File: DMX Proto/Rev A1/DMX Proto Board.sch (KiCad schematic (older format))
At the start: 20 parts, among them J1 XLR5, J2 XLR5, J3 CONN_01X02_MALE, J4 CONN_01X02_MALE, J5 CONN_01X02_MALE, J6 CONN_01X02_MALE, U1 MAX481, U2 MAX481, U3 TCMT1600, U4 TCMT1600

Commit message: change dmx buffer
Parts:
- removed J3: CONN_01X02_MALE, conn_Molex:7395-02, symbol CONN_01X02_MALE
- removed R3, R4, R6, R8: 1K, Resistors_SMD:R_0603_HandSoldering, symbol R
- removed R5, R7: 4K7, Resistors_SMD:R_0603_HandSoldering, symbol R
- removed U1, U2: MAX481, Housings_SOIC:SOIC-8_3.9x4.9mm_Pitch1.27mm, symbol MAX481
- removed U3, U4: TCMT1600, Housings_SSOP:SOP-4_4.4x2.8mm_Pitch1.27mm, symbol TCMT1600
- added U1, U2: ISO35T, Housings_SOIC:SOIC-16_7.5x10.5mm_Pitch1.27mm, symbol ISO35T
- added U?: TPS76333, TO_SOT_Packages_SMD:SOT-23-5, symbol TPS76333
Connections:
- net labels added: +3.3V, +3.3VA, DMX+, DMX-, GNDA, RDM+, RDM-
- net labels removed: +5V, DMX_IN_A, DMX_IN_B, DMX_OUT_A, DMX_OUT_B, DMX_RX, DMX_TX
- wire segments 87 -> 79
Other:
- moved on the sheet: D1, J1, J2, J4, J6, R1, R2, R9

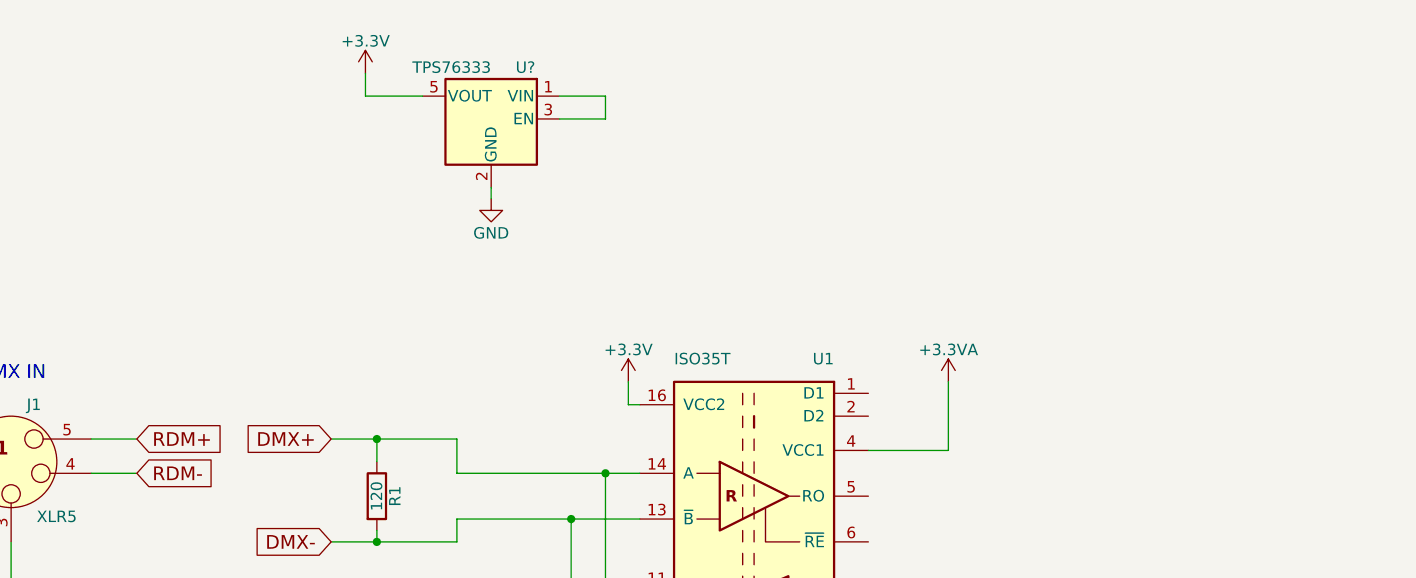
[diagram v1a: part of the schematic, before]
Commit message: Add power isolation to the schematic
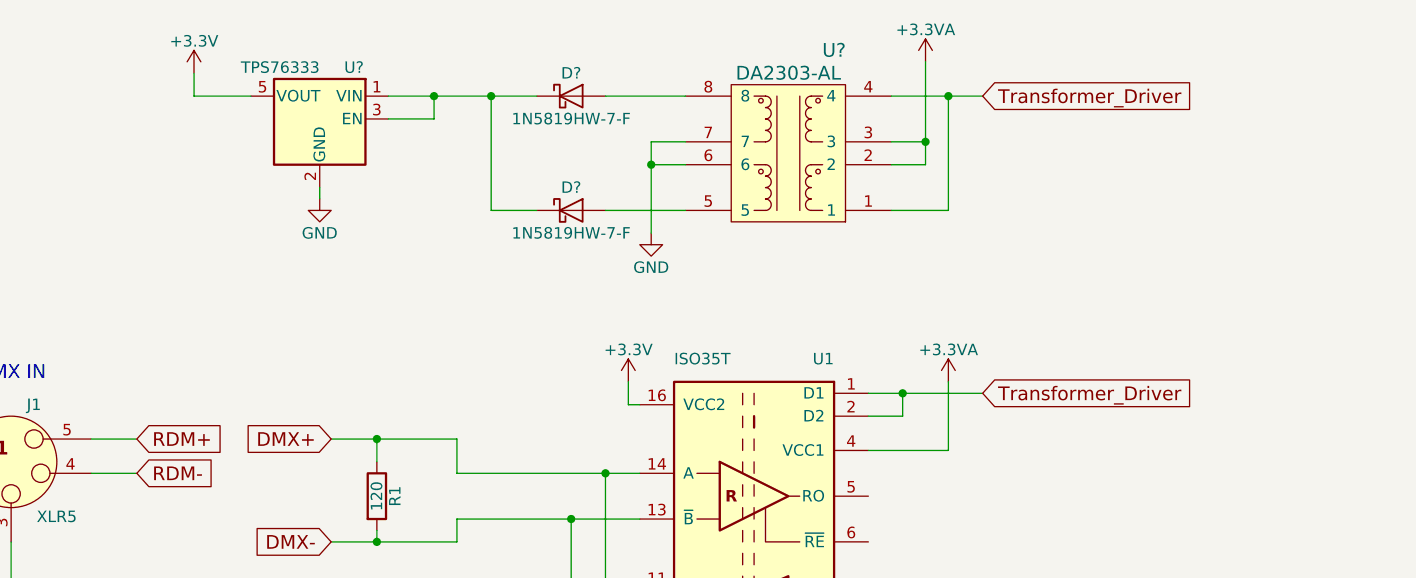
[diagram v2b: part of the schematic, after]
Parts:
- added D? (x2): 1N5819HW-7-F, symbol D_Schottky
- added U?: DA2303-AL, symbol DA2303-AL
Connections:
- net +3.3VA: now also U?.2, U?.3
- net GND: now also U?.6, U?.7
- net Transformer_Driver: now reaches U1.1 (D1)
- net Transformer_Driver: now also U1.2 (D2), U?.1, U?.4
- net at U?.1 (VIN), U?.3 (EN): now also D?.1 (K), D?.1 (K)
- new net: D?.2 (A), U?.5
- new net: D?.2 (A), U?.8
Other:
- moved on the sheet: U?
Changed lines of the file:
@@
 L TPS76333 U?
 U 1 1 596FCFA0
-P 3650 1000
-F 0 "U?" H 3500 1225 50  0000 C CNN
-F 1 "TPS76333" H 3650 1225 50  0000 L CNN
-F 2 "TO_SOT_Packages_SMD:SOT-23-5" H 3650 1325 50  0001 C CIN
-F 3 "" H 3650 1000 50  0001 C CNN
-	1    3650 1000
+P 2900 1000
+F 0 "U?" H 2750 1225 50  0000 C CNN
+F 1 "TPS76333" H 2900 1225 50  0000 L CNN
+F 2 "TO_SOT_Packages_SMD:SOT-23-5" H 2900 1325 50  0001 C CIN
+F 3 "" H 2900 1000 50  0001 C CNN
+	1    2900 1000
 	-1   0    0    -1
 $EndComp
 Wire Wire Line
-	3950 1000 4150 1000
+	3200 1000 3400 1000
 Wire Wire Line
-	4150 1000 4150 900
+	3400 1000 3400 900
 Wire Wire Line
-	4150 900  3950 900
+	3200 900  3850 900
 $Comp
 L GND #PWR?
 U 1 1 596FD867
-P 3650 1350
-F 0 "#PWR?" H 3650 1100 50  0001 C CNN
-F 1 "GND" H 3650 1200 50  0000 C CNN
-F 2 "" H 3650 1350 50  0001 C CNN
-F 3 "" H 3650 1350 50  0001 C CNN
-	1    3650 1350
+P 2900 1350
+F 0 "#PWR?" H 2900 1100 50  0001 C CNN
+F 1 "GND" H 2900 1200 50  0000 C CNN
+F 2 "" H 2900 1350 50  0001 C CNN
+F 3 "" H 2900 1350 50  0001 C CNN
+	1    2900 1350
 	1    0    0    -1
 $EndComp
@@
 L +3.3V #PWR?
 U 1 1 596FD8F6
-P 3100 800
-F 0 "#PWR?" H 3100 650 50  0001 C CNN
-F 1 "+3.3V" H 3100 940 50  0000 C CNN
-F 2 "" H 3100 800 50  0001 C CNN
-F 3 "" H 3100 800 50  0001 C CNN
-	1    3100 800
+P 2350 800
+F 0 "#PWR?" H 2350 650 50  0001 C CNN
+F 1 "+3.3V" H 2350 940 50  0000 C CNN
+F 2 "" H 2350 800 50  0001 C CNN
+F 3 "" H 2350 800 50  0001 C CNN
+	1    2350 800
 	1    0    0    -1
 $EndComp
 Wire Wire Line
-	3100 800  3100 900
+	2350 800  2350 900
 Wire Wire Line
-	3100 900  3350 900
+	2350 900  2600 900
 Wire Wire Line
-	3650 1350 3650 1300
+	2900 1350 2900 1300
 $Comp
 L GNDA #PWR?
@@
 	1    0    0    -1
 $EndComp
+$Comp
+L DA2303-AL U?
+U 1 1 597087A0
+P 4950 1450
+F 0 "U?" H 4750 2200 60  0000 C CNN
+F 1 "DA2303-AL" H 4950 2100 60  0000 C CNN
+F 2 "" H 5000 1450 60  0001 C CNN
+F 3 "" H 5000 1450 60  0001 C CNN
+	1    4950 1450
+	-1   0    0    -1
+$EndComp
+$Comp
+L GND #PWR?
+U 1 1 597089F1
+P 4350 1500
+F 0 "#PWR?" H 4350 1250 50  0001 C CNN
+F 1 "GND" H 4350 1350 50  0000 C CNN
+F 2 "" H 4350 1500 50  0001 C CNN
+F 3 "" H 4350 1500 50  0001 C CNN
+	1    4350 1500
+	1    0    0    -1
+$EndComp
+Wire Wire Line
+	4350 1500 4350 1100
+Wire Wire Line
+	4350 1100 4500 1100
+Wire Wire Line
+	4500 1200 4350 1200
+Connection ~ 4350 1200
+Wire Wire Line
+	5400 1100 5550 1100
+Wire Wire Line
+	5550 750  5550 1200
+Wire Wire Line
+	5550 1200 5400 1200
+Connection ~ 5550 1100
+$Comp
+L +3.3VA #PWR?
+U 1 1 59708F23
+P 5550 750
+F 0 "#PWR?" H 5550 600 50  0001 C CNN
+F 1 "+3.3VA" H 5550 890 50  0000 C CNN
+F 2 "" H 5550 750 50  0001 C CNN
+F 3 "" H 5550 750 50  0001 C CNN
+	1    5550 750
+	1    0    0    -1
+$EndComp
+Wire Wire Line
+	5300 2200 5800 2200
+Wire Wire Line
+	5450 2200 5450 2300
+Wire Wire Line
+	5450 2300 5300 2300
+Text GLabel 5800 2200 2    60   Input ~ 0
+Transformer_Driver
+Text GLabel 5800 900  2    60   Input ~ 0
+Transformer_Driver
+Wire Wire Line
+	5400 900  5800 900
+Wire Wire Line
+	5400 1400 5650 1400
+Wire Wire Line
+	5650 1400 5650 900
+Connection ~ 5650 900
+Connection ~ 5450 2200
+$Comp
+L D_Schottky D?
+U 1 1 597099FD
+P 4000 900
+F 0 "D?" H 4000 1000 50  0000 C CNN
+F 1 "1N5819HW-7-F" H 4000 800 50  0000 C CNN
+F 2 "" H 4000 900 50  0001 C CNN
+F 3 "" H 4000 900 50  0001 C CNN
+	1    4000 900
+	1    0    0    -1
+$EndComp
+$Comp
+L D_Schottky D?
+U 1 1 59709A5E
+P 4000 1400
+F 0 "D?" H 4000 1500 50  0000 C CNN
+F 1 "1N5819HW-7-F" H 4000 1300 50  0000 C CNN
+F 2 "" H 4000 1400 50  0001 C CNN
+F 3 "" H 4000 1400 50  0001 C CNN
+	1    4000 1400
+	1    0    0    -1
+$EndComp
+Wire Wire Line
+	4150 1400 4500 1400
+Wire Wire Line
+	3850 1400 3650 1400
+Wire Wire Line
+	3650 1400 3650 900
+Wire Wire Line
+	4150 900  4500 900
+Connection ~ 3400 900
+Connection ~ 3650 900
 $EndSCHEMATC

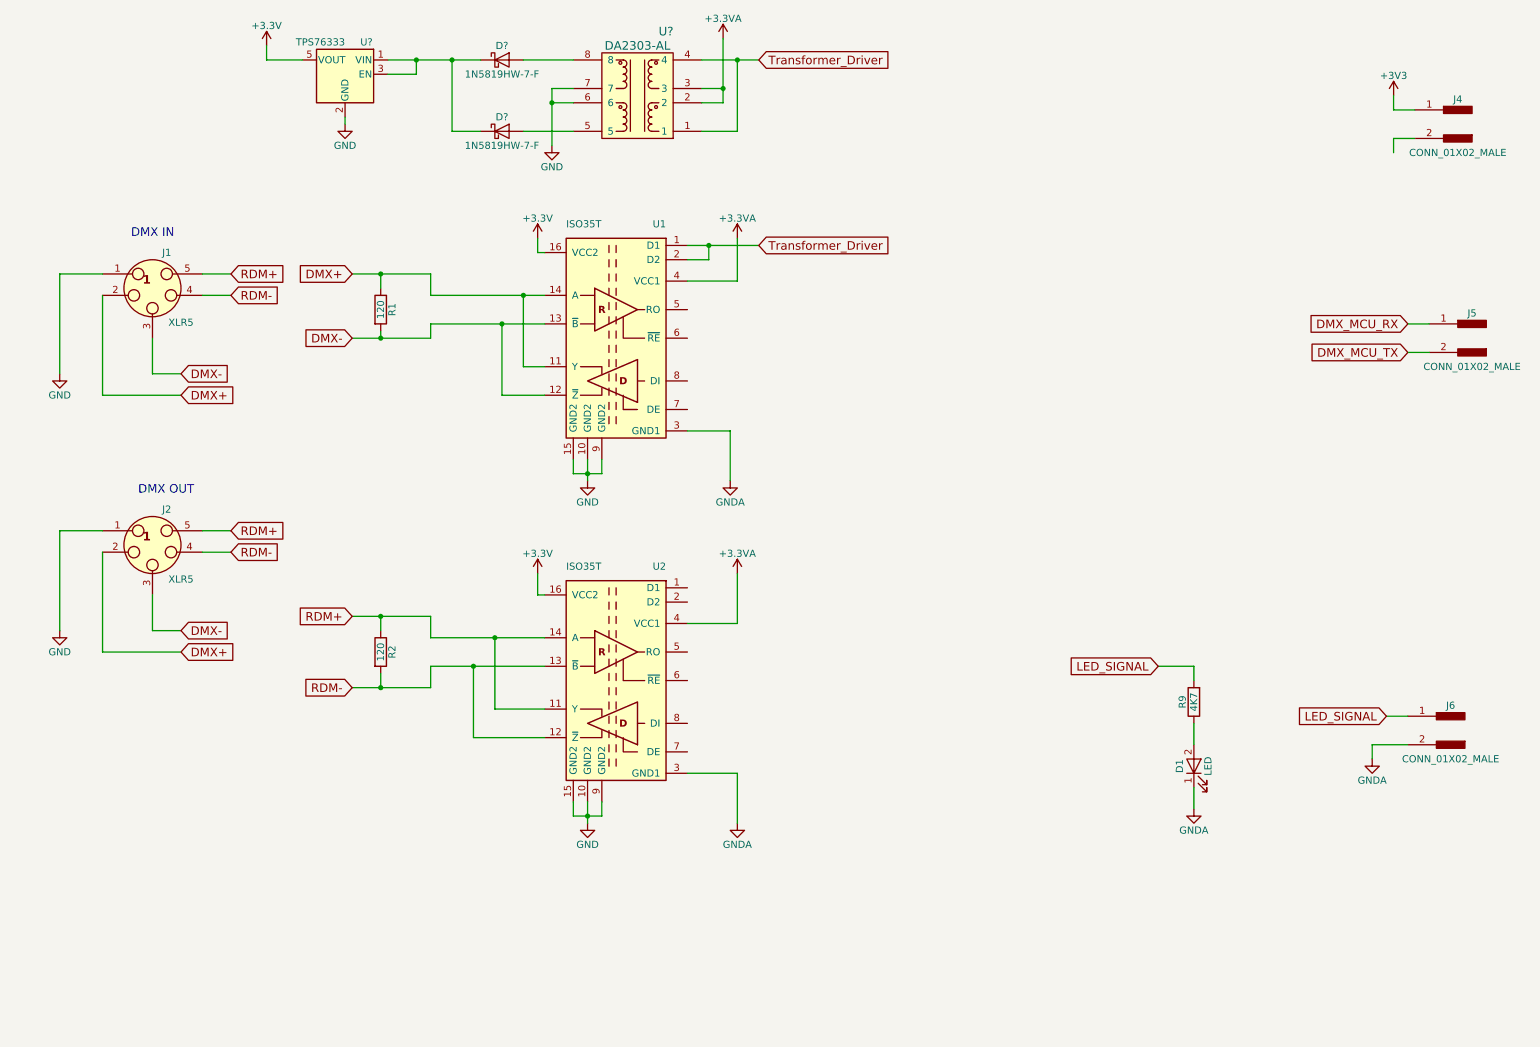
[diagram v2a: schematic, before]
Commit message: Add capsitor on the power
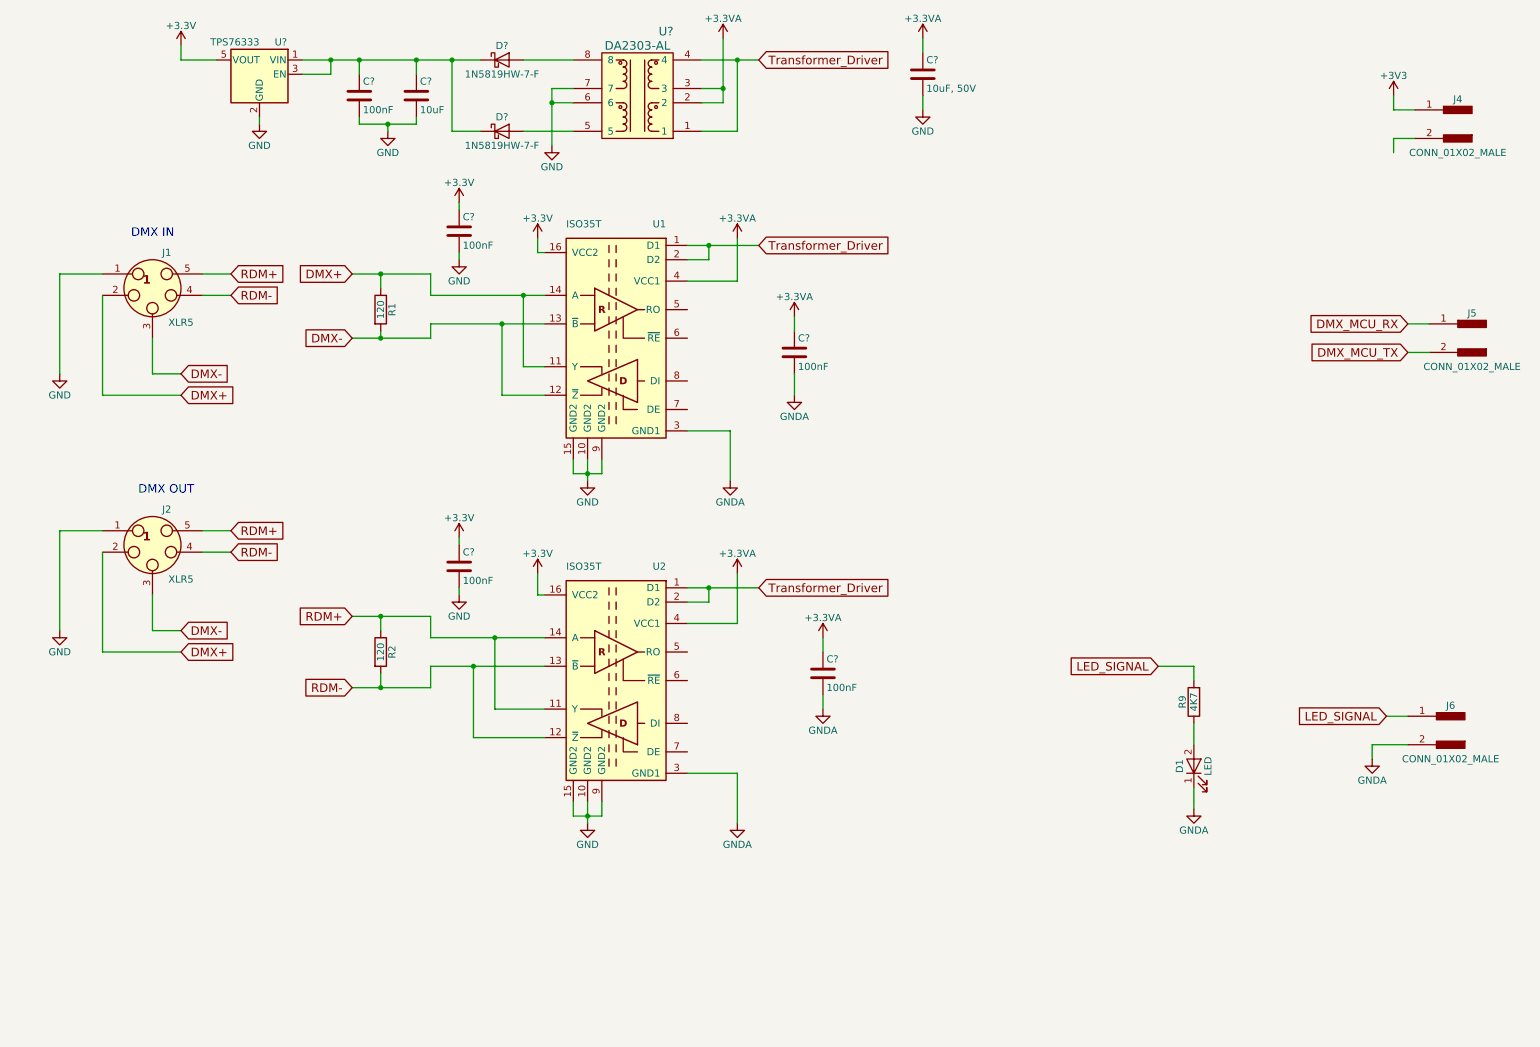
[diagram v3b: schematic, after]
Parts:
- added C?: 10uF, 50V, symbol C
- added C? (x5): 100nF, symbol C
- added C?: 10uF, symbol C
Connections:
- net +3.3VA: now also C?.1, C?.1, C?.1
- net +3V3: now also C?.1, C?.1
- net GND: now also C?.2, C?.2, C?.2, C?.2, C?.2
- net GNDA: now also C?.2, C?.2
- net Transformer_Driver: now also U2.1 (D1), U2.2 (D2)
- net at D?.1 (K), D?.1 (K), U?.1 (VIN)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: now also C?.1, C?.1
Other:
- moved on the sheet: U?

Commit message: Add Transint proction and name's net of the output
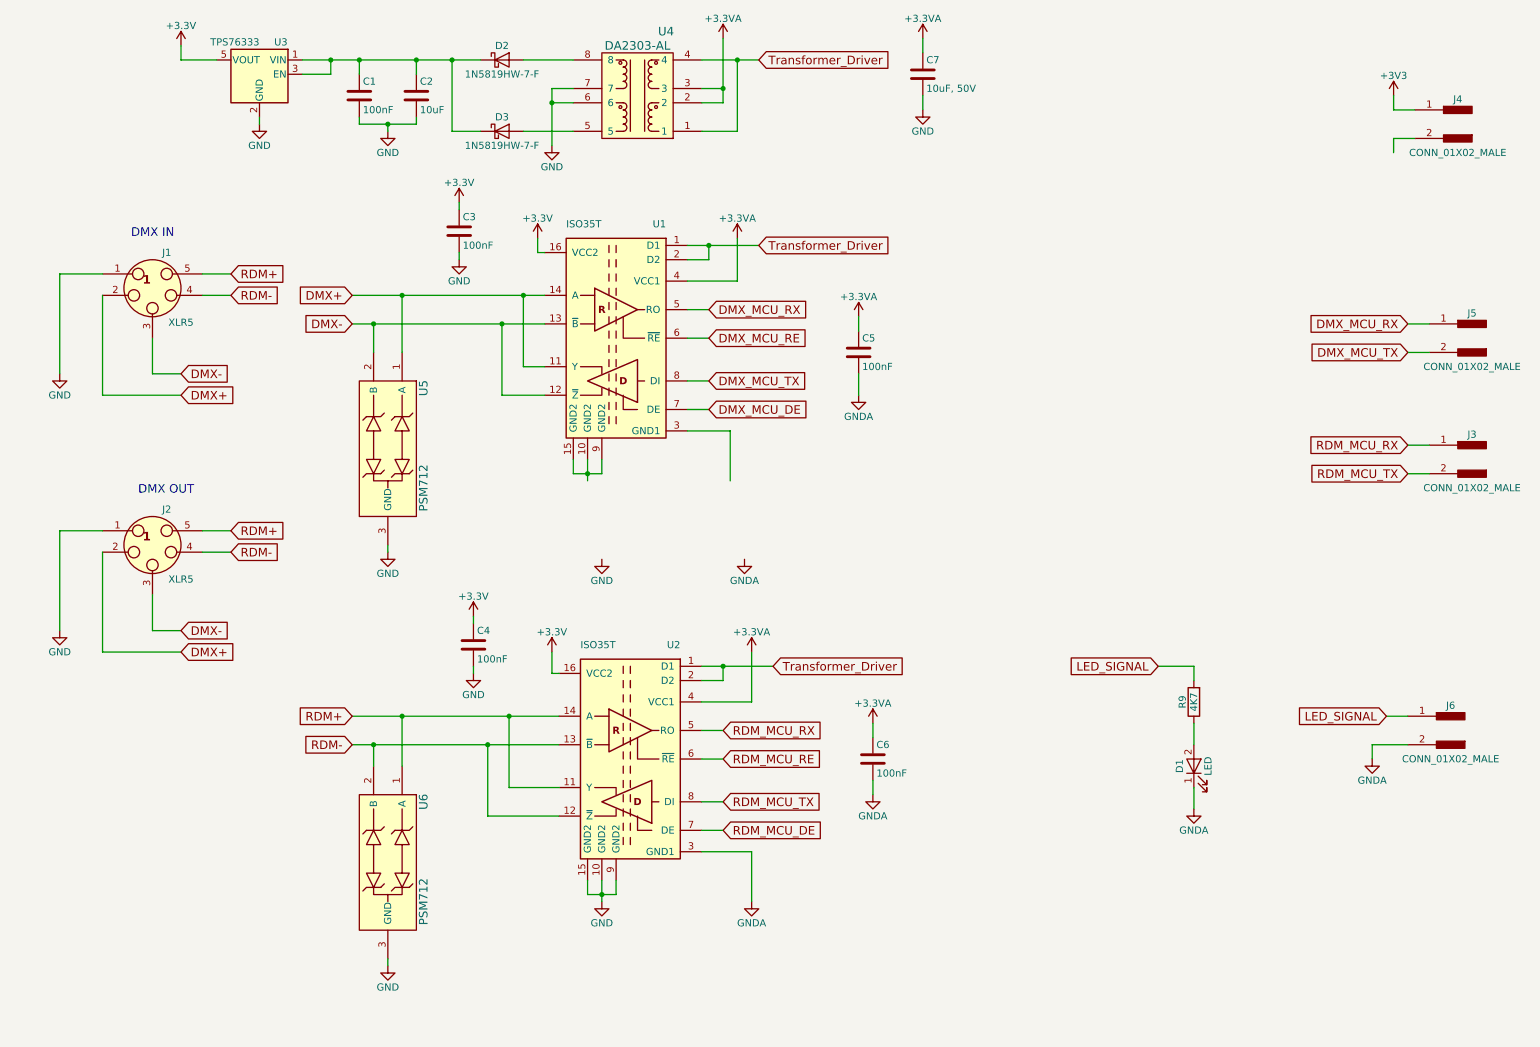
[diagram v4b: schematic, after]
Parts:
- removed R1, R2: 120, Resistors_SMD:R_0603_HandSoldering, symbol R
- added J3: CONN_01X02_MALE, conn_Molex:7395-02, symbol CONN_01X02_MALE
- added U5, U6: PSM712, symbol PSM712
- gave numbers to parts that had none: 11
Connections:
- net DMX+: now also U5.1 (A)
- net DMX-: now also U5.2 (B)
- net DMX_MCU_RX: now also U1.5 (RO)
- net DMX_MCU_TX: now also U1.8 (DI)
- net GND: now also U5.3 (GND), U6.3 (GND); no longer U1.10 (GND2), U1.15 (GND2), U1.9 (GND2)
- net GNDA: no longer U1.3 (GND1)
- net RDM+: now also U6.1 (A)
- net RDM-: now also U6.2 (B)
- net DMX_MCU_RE: now reaches U1.6 (~RE)
- net DMX_MCU_DE: now reaches U1.7 (DE)
- net RDM_MCU_RX: now reaches U2.5 (RO)
- net RDM_MCU_RX: now also J3.1
- net RDM_MCU_RE: now reaches U2.6 (~RE)
- net RDM_MCU_DE: now reaches U2.7 (DE)
- net RDM_MCU_TX: now reaches U2.8 (DI)
- net RDM_MCU_TX: now also J3.2
- new net: U1.10 (GND2), U1.15 (GND2), U1.9 (GND2)
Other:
- moved on the sheet: C4, C5, C6, U2

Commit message: Route the board and generate gerber
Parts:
- removed J1: XLR5, Neutrix:NC5MAV-SW, symbol XLR5
- removed J2: XLR5, Neutrix:NC5FAV-SW, symbol XLR5
- removed J3, J5: CONN_01X02_MALE, conn_Molex:7395-02, symbol CONN_01X02_MALE
- added J1: NC5MAH, Neutrix:NC5MAV-SW, symbol XLR5-N
- added J2: NC5FAH, Neutrix:NC5FAV-SW, symbol XLR5-N
- added J3, J5: 22-05-7048, Sockets_MOLEX_KK-System:Socket_MOLEX-KK-RM2-54mm_Lock_4pin_straight, symbol CONN_01X04_MALE
- added R1, R2: 120R, Resistors_SMD:R_0603_HandSoldering, symbol R
- added R3: 1K, Resistors_SMD:R_0603_HandSoldering, symbol R
- added U7: MAX4751, Housings_SSOP:TSSOP-14_4.4x5mm_Pitch0.65mm, symbol MAX4751
- C1, C3, C4, C5, C6: footprint (none) -> Capacitors_SMD:C_0603_HandSoldering
- C2, C7: footprint (none) -> Capacitors_SMD:C_0805_HandSoldering
- D2, D3: footprint (none) -> Diodes_SMD:D_SOD-123
- J4, J6: value CONN_01X02_MALE -> 22-05-7028
- U1, U2: footprint Housings_SOIC:SOIC-16_7.5x10.5mm_Pitch1.27mm -> Housings_SOIC:SOIC-16_3.9x9.9mm_Pitch1.27mm
- U4: footprint (none) -> CoilCraft:transformer-8-10x12.07
- U5, U6: footprint (none) -> TO_SOT_Packages_SMD:SOT-23
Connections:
- net +3.3VA: now also J4.1
- net +3V3: now also R3.1, U7.14 (Vcc); no longer J4.1
- net DMX+: now also J1.2 (P2), J2.2 (P2), U7.2 (COM1)
- net DMX-: now also J1.3 (P3), J2.3 (P3), U7.3 (NO2)
- net DMX_MCU_DE: now also J3.3
- net DMX_MCU_RE: now also J3.2
- net DMX_MCU_RX: now also J3.1
- net DMX_MCU_TX: now also J3.4
- net GND: now also U1.10 (GND2), U1.15 (GND2), U1.9 (GND2), J1.1 (P1), J2.1 (P1), U7.7 (GND); no longer C7.2
- net GNDA: now also C7.2, J4.2, U1.3 (GND1)
- net RDM+: now also J1.5 (P5), J2.5 (P5), U7.9 (COM3)
- net RDM-: now also J1.4 (P3), J2.4 (P3), U7.10 (COM4)
- net RDM_MCU_DE: now also J5.3
- net RDM_MCU_RE: now also J5.2
- net RDM_MCU_RX: now also J5.1
- net RDM_MCU_TX: now also J5.4
- net Transformer_Driver renamed Transformer_Driver_1
- net Transformer_Driver_1: no longer U1.2 (D2), U2.2 (D2), U4.1
- new net: R1.1, U7.1 (NO1)
- new net: R1.2, U7.4 (COM2)
- new net: R2.1, U7.8 (NO3)
- new net: R2.2, U7.11 (NO4)
- new net: J1.NC, U7.12 (IN4), U7.13 (IN1), U7.5 (IN2), U7.6 (IN3)
- new net: J1.N, R3.2
- new net Transformer_Driver_2: U1.2 (D2), U2.2 (D2), U4.1
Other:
- moved on the sheet: C1, C2, C3, C4, C5, C6, C7, D2, D3, U1, U2, U3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
